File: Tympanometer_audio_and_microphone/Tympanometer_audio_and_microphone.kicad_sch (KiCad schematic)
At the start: 32 parts, among them J1 Conn_01x03, J2 Conn_01x02, U1 LM4810, U2 ${SIM.PARAMS}, U3 ${SIM.PARAMS}

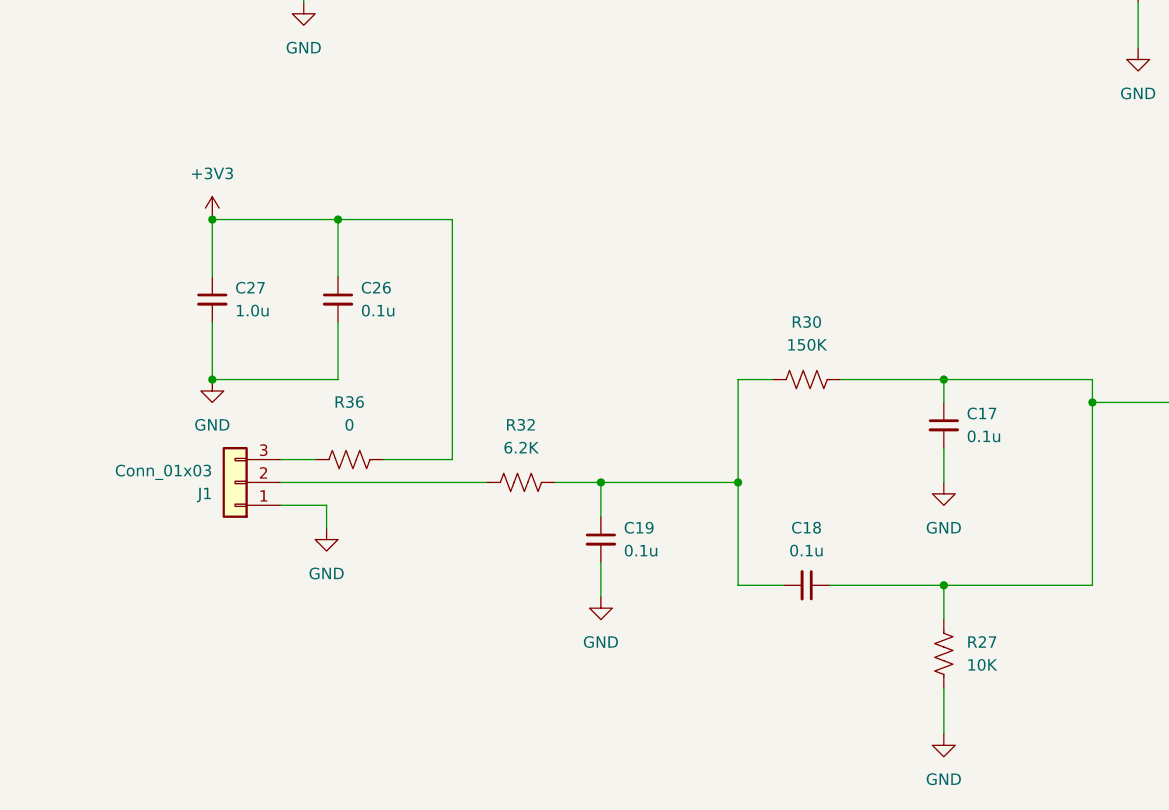
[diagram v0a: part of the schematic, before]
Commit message: integrated VPWL for microphone testing
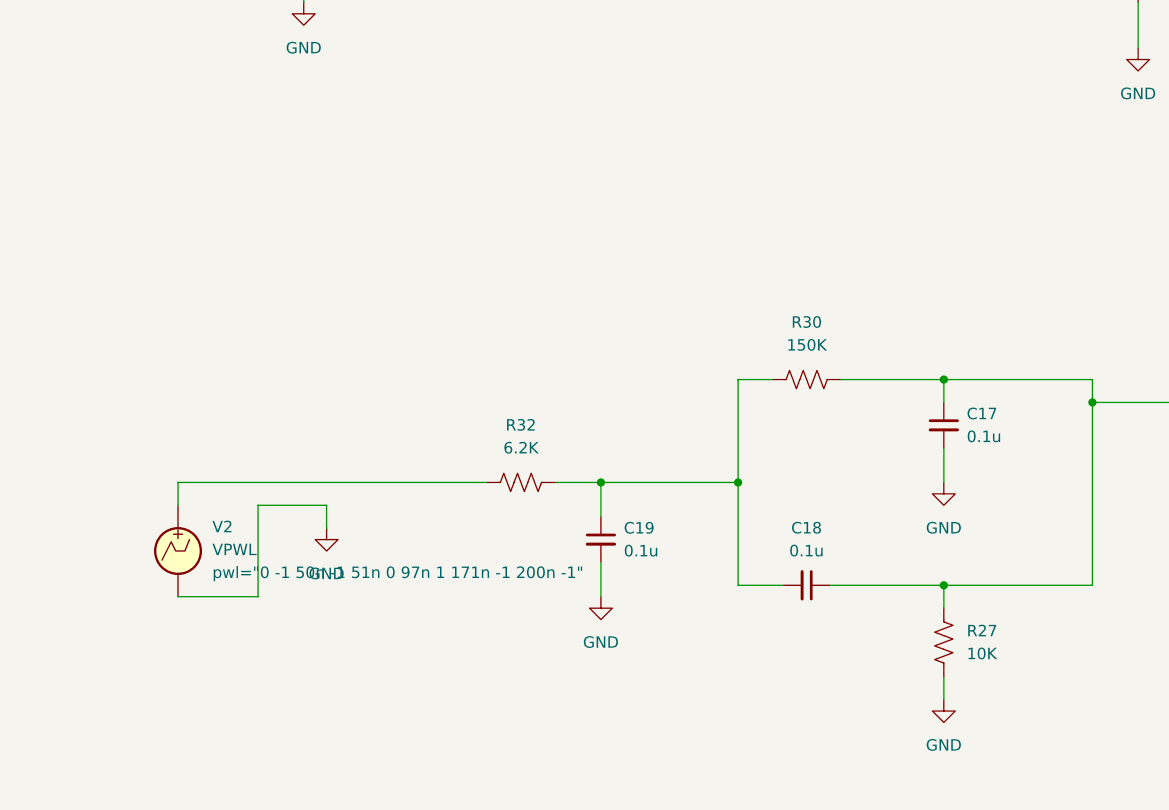
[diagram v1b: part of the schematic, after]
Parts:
- removed C26: 0.1u, symbol Device:C_Small
- removed C27: 1.0u, symbol Device:C_Small
- removed J1: Conn_01x03, symbol Connector_Generic:Conn_01x03
- removed R36: 0, symbol Device:R_US
- added V2: VPWL, symbol Simulation_SPICE:VPWL
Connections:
- net GND: now also V2.2
- net at R32.2: now also V2.1
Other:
- moved on the sheet: R27
